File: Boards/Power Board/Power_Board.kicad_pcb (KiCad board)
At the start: 2 copper layers, 119 x 54.5 mm, 31 parts, among them J1 Conn_01x02, U1 LM22678TJ-5, U2 LM22678TJ-5

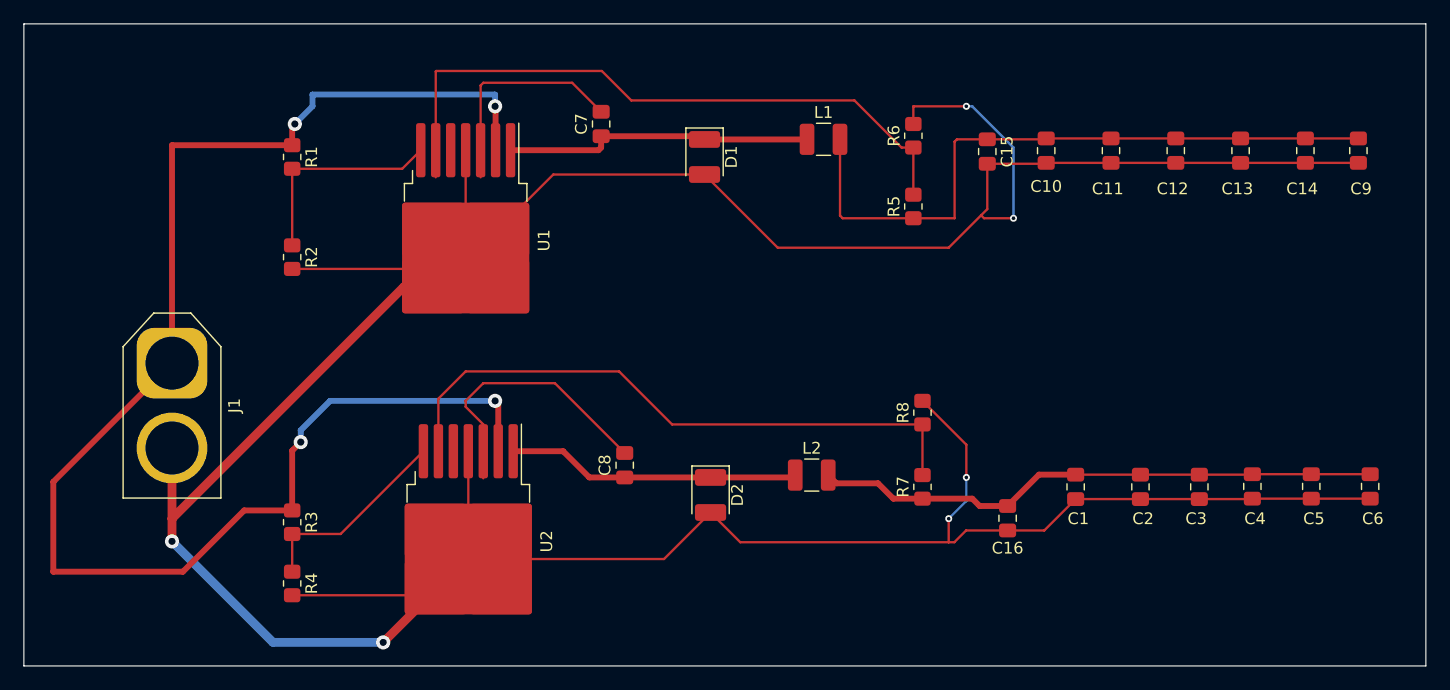
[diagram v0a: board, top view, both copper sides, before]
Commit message: power board connectors and ERC changes
reeeeeeeeeeeeeeeeeeeee
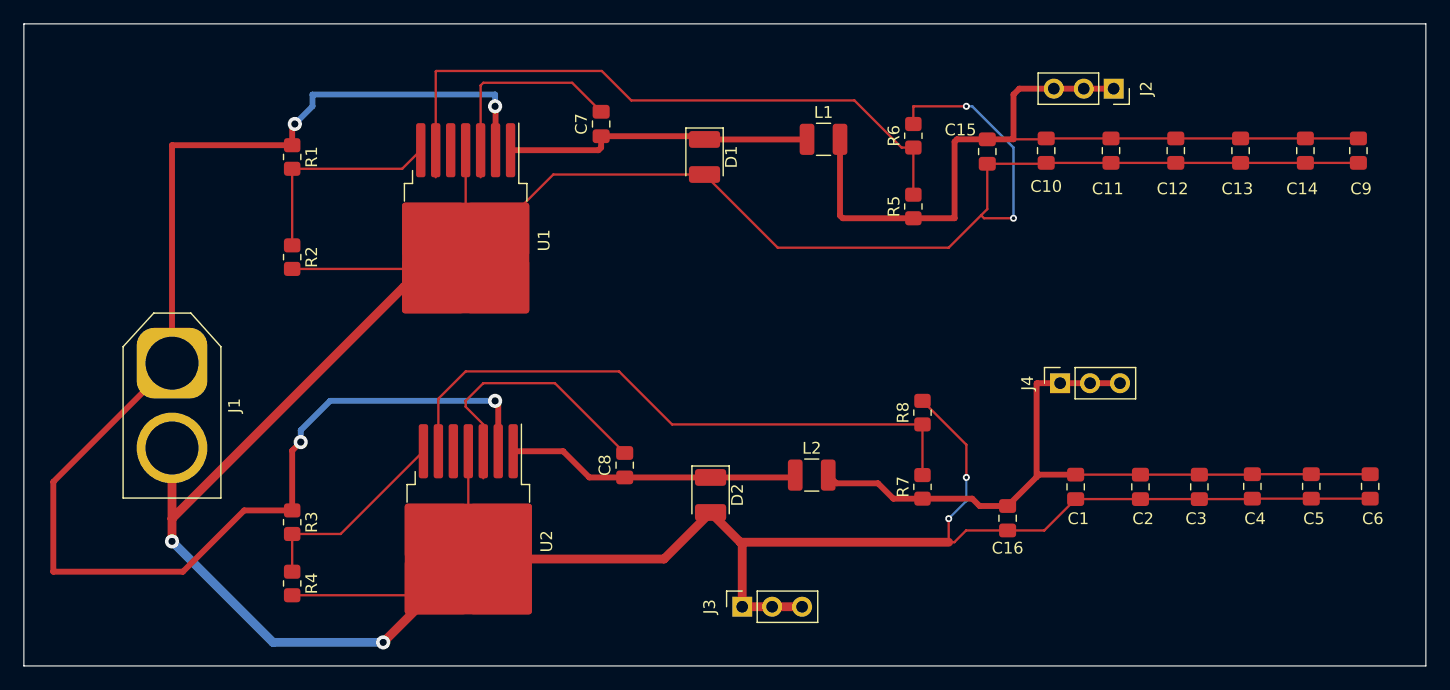
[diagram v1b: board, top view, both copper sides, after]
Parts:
- added J2: Screw_Terminal_01x03, Connector_PinSocket_2.54mm:PinSocket_1x03_P2.54mm_Vertical, F.Cu at (191.5, 57.0)
- added J3: Screw_Terminal_01x03, Connector_PinSocket_2.54mm:PinSocket_1x03_P2.54mm_Vertical, F.Cu at (160.0, 101.0)
- added J4: Screw_Terminal_01x03, Connector_PinSocket_2.54mm:PinSocket_1x03_P2.54mm_Vertical, F.Cu at (187.0, 82.0)
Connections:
- net +3.3V renamed /+3.3V
- net +5V renamed /+5V
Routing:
- net /+3.3V: track 48.2 -> 63.2 mm
- net /+5V: track 57.2 -> 69.7 mm
- net GND: track 320.8 -> 331.4 mm

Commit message: power system size decrease
a
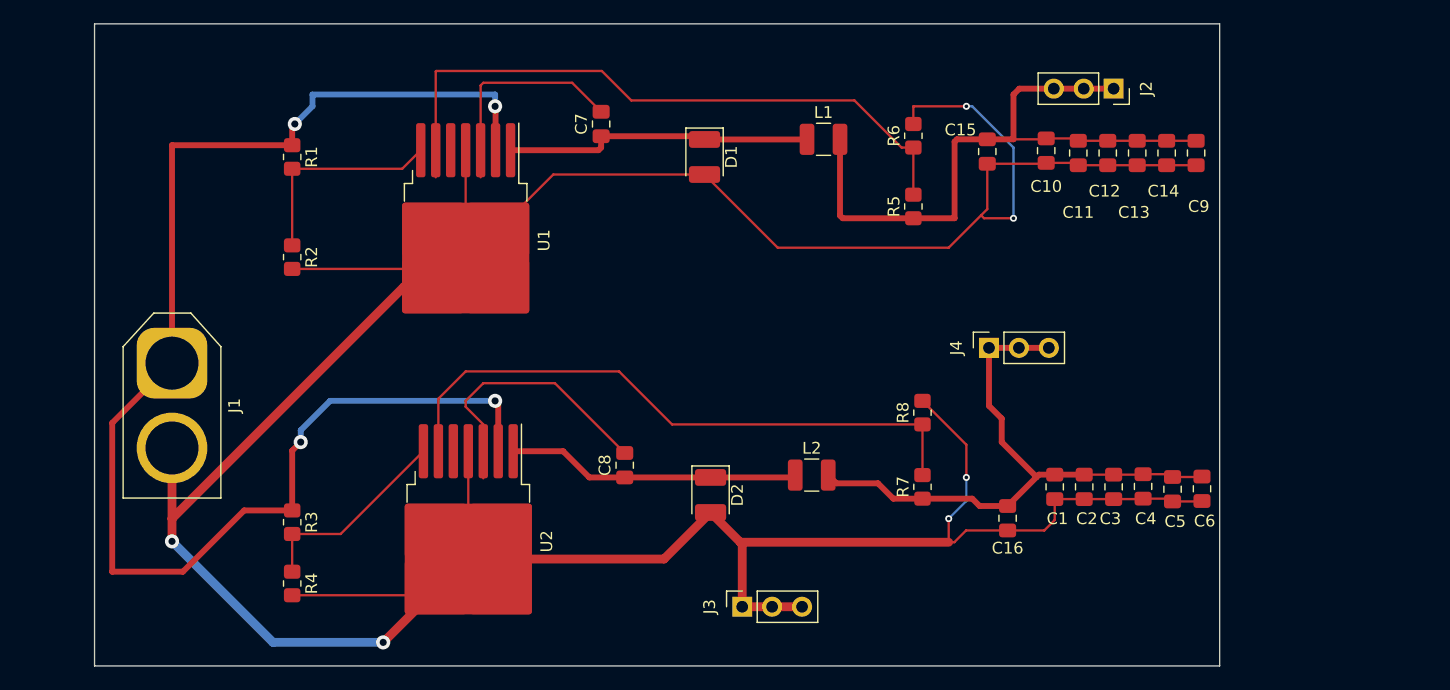
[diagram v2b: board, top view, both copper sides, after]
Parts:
- moved C6 14.3 mm to (199.0, 91.0)
- moved C9 13.8 mm to (198.5, 62.5)
- moved C5 11.8 mm to (196.5, 91.0)
- moved C14 11.8 mm to (196.0, 62.5)
- moved C4 9.28 mm to (194.0, 90.8)
- moved C13 8.78 mm to (193.5, 62.5)
- moved C3 7.28 mm to (191.5, 90.8)
- moved J4 6.74 mm to (180.9, 79.0)
- moved C12 5.78 mm to (191.0, 62.5)
- moved C2 4.78 mm to (189.0, 90.8)
- moved C11 2.78 mm to (188.5, 62.5)
- moved C1 1.78 mm to (186.5, 90.8)
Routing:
- net GND: track 331.4 -> 304.7 mm
- net /+5V: track 69.7 -> 56.0 mm
- net /+3.3V: track 63.2 -> 51.0 mm
- net +7.5V: track 127.3 -> 120.2 mm
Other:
- board size 119 x 54.5 mm -> 95.5 x 54.5 mm
